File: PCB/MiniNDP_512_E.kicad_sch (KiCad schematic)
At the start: 17 parts, among them J1 Conn_02x20_Odd_Even, U1 HC138, U2 4040, U3 FCT821, U4 AS6C4008, U5 2G04, U6 1G32

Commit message: E board
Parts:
- removed C4, C5: 1u, 000_LOCAL:C_0805, symbol 000_LOCAL:C
- removed U2: 4040, 000_LOCAL:SOIC-16_3.9x9.9mm_P1.27mm, symbol 000_LOCAL:4040
- removed U3: FCT821, 000_LOCAL:SOIC-24, symbol 000_LOCAL:74xx821
- removed U4: AS6C4008, 000_LOCAL:TSOP-II-SOP-32_dual, symbol 000_LOCAL:AS6C4008_DIP
- removed U5: 2G04, 000_LOCAL:SOT-363_SC-70-6, symbol 000_LOCAL:2G04
- added C2, C3, C6, C7: 1u, 000_LOCAL:C_0805, symbol 000_LOCAL:C
- added JP1: 256k, 000_LOCAL:SolderJumper-2_Open 0.65mm, symbol 000_LOCAL:SolderJumper_2_Open
- added U1, U2, U3: HC161, 000_LOCAL:TSSOP-16, symbol 000_LOCAL:74xx161
- added U5: 74xx574, 000_LOCAL:TSSOP-20, symbol 000_LOCAL:74xx574
- added U6: AS6C4008, 000_LOCAL:TSOP32-dual, symbol 000_LOCAL:AS6C4008_TSOP
- added U8: 1G79, 000_LOCAL:SOT-353_SC-70-5, symbol 000_LOCAL:74xx1G79
- U4: renamed from U1; footprint 000_LOCAL:SOIC-16_3.9x9.9mm_P1.27mm -> 000_LOCAL:TSSOP-16
- renumbered C2 to C4, C3 to C5, U6 to U7
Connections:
- net A0: now also U1.14 (Q0), U6.15 (A5)
- net A1: now also U1.13 (Q1), U6.14 (A6)
- net A10: now also U5.19 (Q0), U6.11 (A14)
- net A11: now also U5.18 (Q1), U6.10 (A16)
- net A12: now also U5.17 (Q2), U6.7 (A15)
- net A13: now also U5.16 (Q3), U6.4 (A13)
- net A14: now also U5.15 (Q4), U6.3 (A8)
- net A15: now also U5.14 (Q5), U6.2 (A9)
- net A16: now also U5.13 (Q6), U6.1 (A11)
- net A17: now also U5.12 (Q7), U6.9 (A18)
- net A18: now also JP1.2 (B), U6.6 (A17), U8.4 (Q)
- net A2: now also U1.12 (Q2), U6.13 (A7)
- net A3: now also U1.11 (Q3), U6.12 (A12)
- net A4: now also U2.14 (Q0), U6.19 (A1)
- net A5: now also U2.13 (Q1), U6.20 (A0)
- net A6: now also U2.12 (Q2), U6.31 (A10)
- net A7: now also U2.11 (Q3), U6.16 (A4)
- net A8: now also U3.14 (Q0), U6.17 (A3)
- net A9: now also U3.13 (Q1), U6.18 (A2)
- net AD0: now also U5.2 (D0), U6.21 (Q0)
- net AD1: now also U5.3 (D1), U6.22 (Q1)
- net AD2: now also U5.4 (D2), U6.23 (Q2)
- net AD3: now also U5.5 (D3), U6.25 (Q3)
- net AD4: now also U5.6 (D4), U6.26 (Q4)
- net AD5: now also U5.7 (D5), U6.27 (Q5)
- net AD6: now also U5.8 (D6), U6.28 (Q6)
- net AD7: now also U5.9 (D7), U6.29 (Q7)
- net BUS_A10: now also U8.1 (D)
- net GND: now also U4.4 (E1), C2.2, C3.2, C6.2, C7.2, U1.3 (D0), U1.4 (D1), U1.5 (D2), U1.6 (D3), U1.8 (GND), U2.3 (D0), U2.4 (D1), U2.5 (D2), U2.6 (D3), U2.8 (GND), U3.3 (D0), U3.4 (D1), U3.5 (D2), U3.6 (D3), U3.8 (GND), U5.1 (OE), U5.10 (GND), U6.24 (GND), U8.3 (GND); no longer U4.5 (E2)
- net SLEEP: now also U7.2; no longer U7.1
- net VBUS: now also C3.1, C6.1, C7.1, JP1.1 (A), U1.10 (CET), U1.16 (VCC), U1.7 (CEP), U1.9 (~{PE}), U2.16 (VCC), U2.9 (~{PE}), U3.16 (VCC), U3.9 (~{PE}), U5.20 (VCC), U8.5 (VCC)
- net VMEM: now also C2.1, U6.8 (VCC)
- net ~{BLOCK}: now also U1.1 (~{MR}), U2.1 (~{MR}), U3.1 (~{MR}), U5.11 (Cp), U8.2 (C)
- net ~{BYTE}: now also U7.1, U1.2 (CP), U2.2 (CP), U3.2 (CP); no longer U7.2
- net ~{CE}: now also U6.30 (~{CE})
- net ~{RD}: now also U6.32 (~{OE})
- net ~{WR}: now also U6.5 (~{WE})
- net ~{Y0}: now also U4.5 (E2); no longer U4.4 (E1)
- new net TC0: U1.15 (TC), U2.10 (CET), U2.7 (CEP)
- new net TC1: U2.15 (TC), U3.10 (CET), U3.7 (CEP)
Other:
- note added: "(*)"
- note added: "(*) A17 must be opposite AD7 for 128k compatibility"
- note added: "(**)"
- note added: "(**) A18 must be on pin 6 for 256k or 128k compatibility A17 must be on pin 9 for 128k compatibility"
- note added: "For 512k: Populate U8 with 1G79 or 1G80. Keep JP1 Open. Populate U6 with AS6C4008. For 256k or 128k: Don't populate U8. Bridge JP1. Populate U6 with AS6C2008A or AS6C1008."
- note added: "GND"
- note added: "TANDY 100/102/200 BUS (A) ~{YO} A8 A9 A10 -> ~{BLOCK} ~{BYTE} L X X X X X X X H X X X X X X X L X X X X H L H L L -> L H Select BLOCK # from BANK0 H L H L H -> L H Select BLOCK # from BANK1 H L H H X -> H L READ/WRITE BYTE Each ~{BLOCK} pulse low: sets A0-A9 to 0, sets A10-A18 from AD0-AD7 & BUS_A10, then holds A10-A18 latched while high. Each ~{BYTE} pulse low: enables SRAM for read or write whi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"
- note removed: "A19"
- note removed: "SOP-32 or TSOP-II-32"
- note removed: "TANDY 100/102/200 BUS (A) ~{YO} A8 A9 A10 -> ~{BLOCK} ~{BYTE} L X X X X X X X H X X X X X X X L X X X X H L H L L -> L H Select BLOCK # from BANK0 H L H L H -> L H Select BLOCK # from BANK1 H L H H X -> H L READ/WRITE BYTE Each ~{BLOCK} pulse low: sets SRAM A0-A9 to 0 sets SRAM A10-A19 from BUS AD0-AD7 & A10 (AD0-AD7 = block#, BUS_A10 = bank#) On returning high: holds SRAM A10-A19 latched while h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"
- moved on the sheet: BT1, C1, C4, C5, DA1A, DA1B, J1, R1, R2, U4, U7

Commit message: E board
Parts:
- U5: value 74xx574 -> HC574
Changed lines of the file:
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@@
 			)
 		)
-		(property "Value" "74xx574"
+		(property "Value" "HC574"
 			(at 154.5941 97.79 0)
 			(effects
@@
 			)
 		)
-		(property "Datasheet" "http://www.ti.com/lit/gpn/sn74LS574"
+		(property "Datasheet" "datasheets/HC574.pdf"
 			(at 152.4 115.57 0)
 			(effects

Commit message: E board
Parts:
- removed C6, C7: 1u, 000_LOCAL:C_0805, symbol 000_LOCAL:C
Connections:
- net BUS_A8: now also U4.3 (A2); no longer U4.1 (A0)
- net GND: now also U4.1 (A0), U4.5 (E2); no longer U4.3 (A2), U4.4 (E1)
- net ~{BLOCK}: now also U4.11 (O4); no longer U4.14 (O1)
- net ~{BYTE}: now also U4.9 (O6); no longer U4.12 (O3)
- net ~{Y0}: now also U4.4 (E1); no longer U4.5 (E2)
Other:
- moved on the sheet: C3, C4, C5, U4

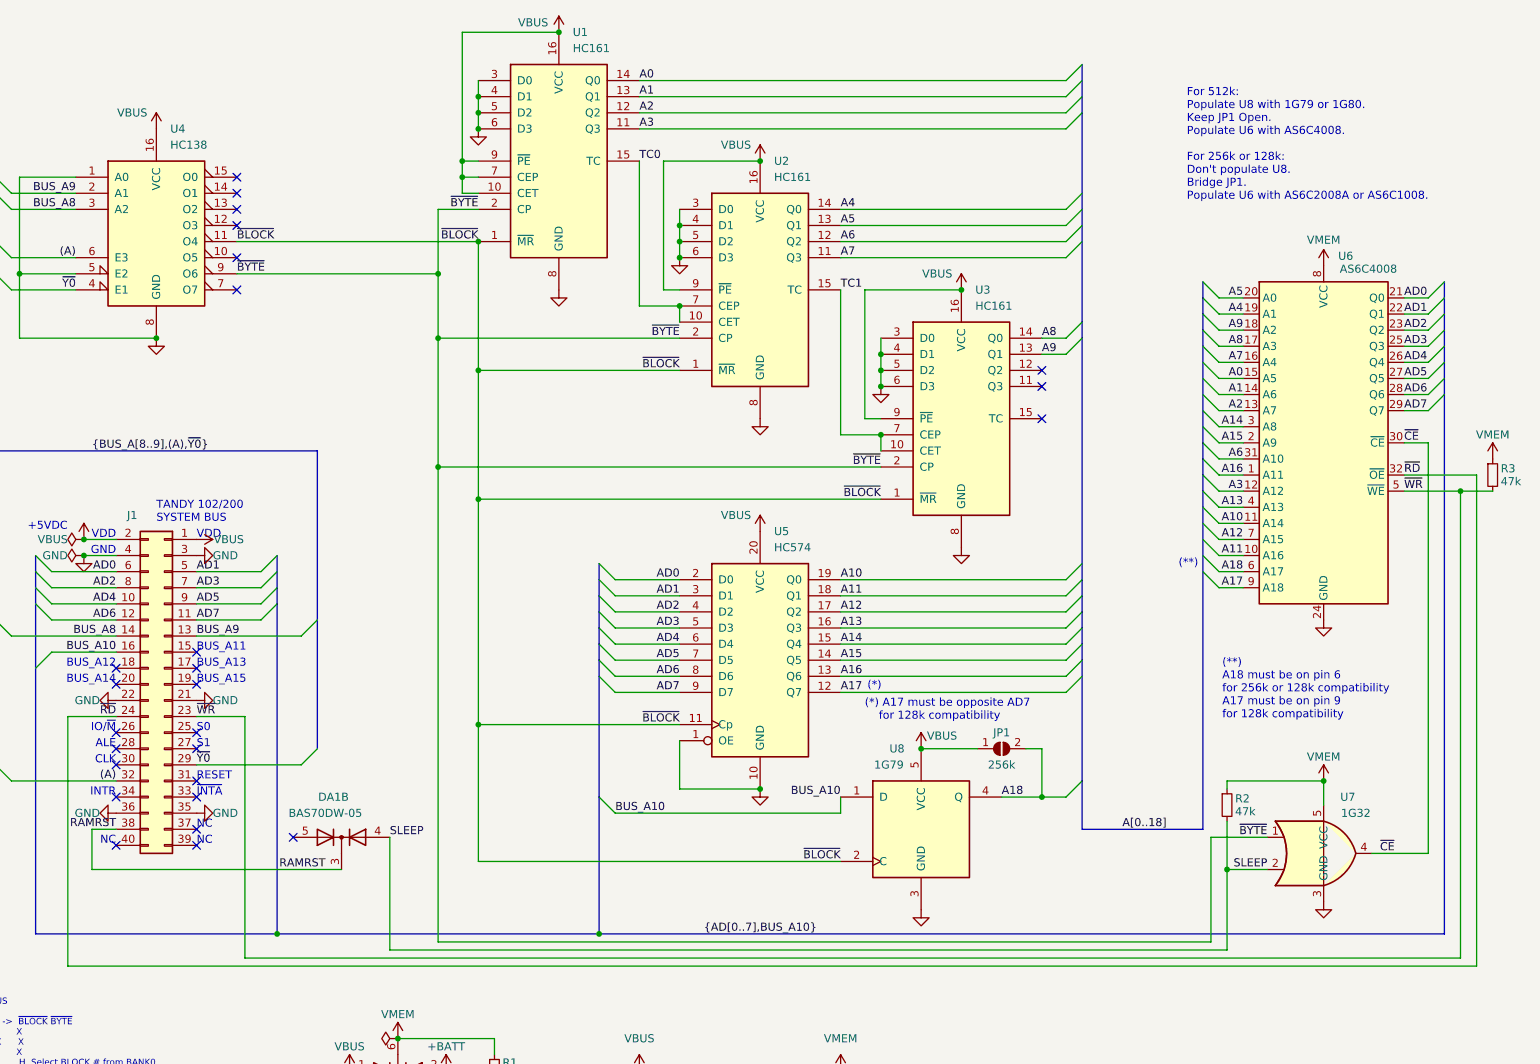
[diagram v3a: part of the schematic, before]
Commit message: E board minor trace positions
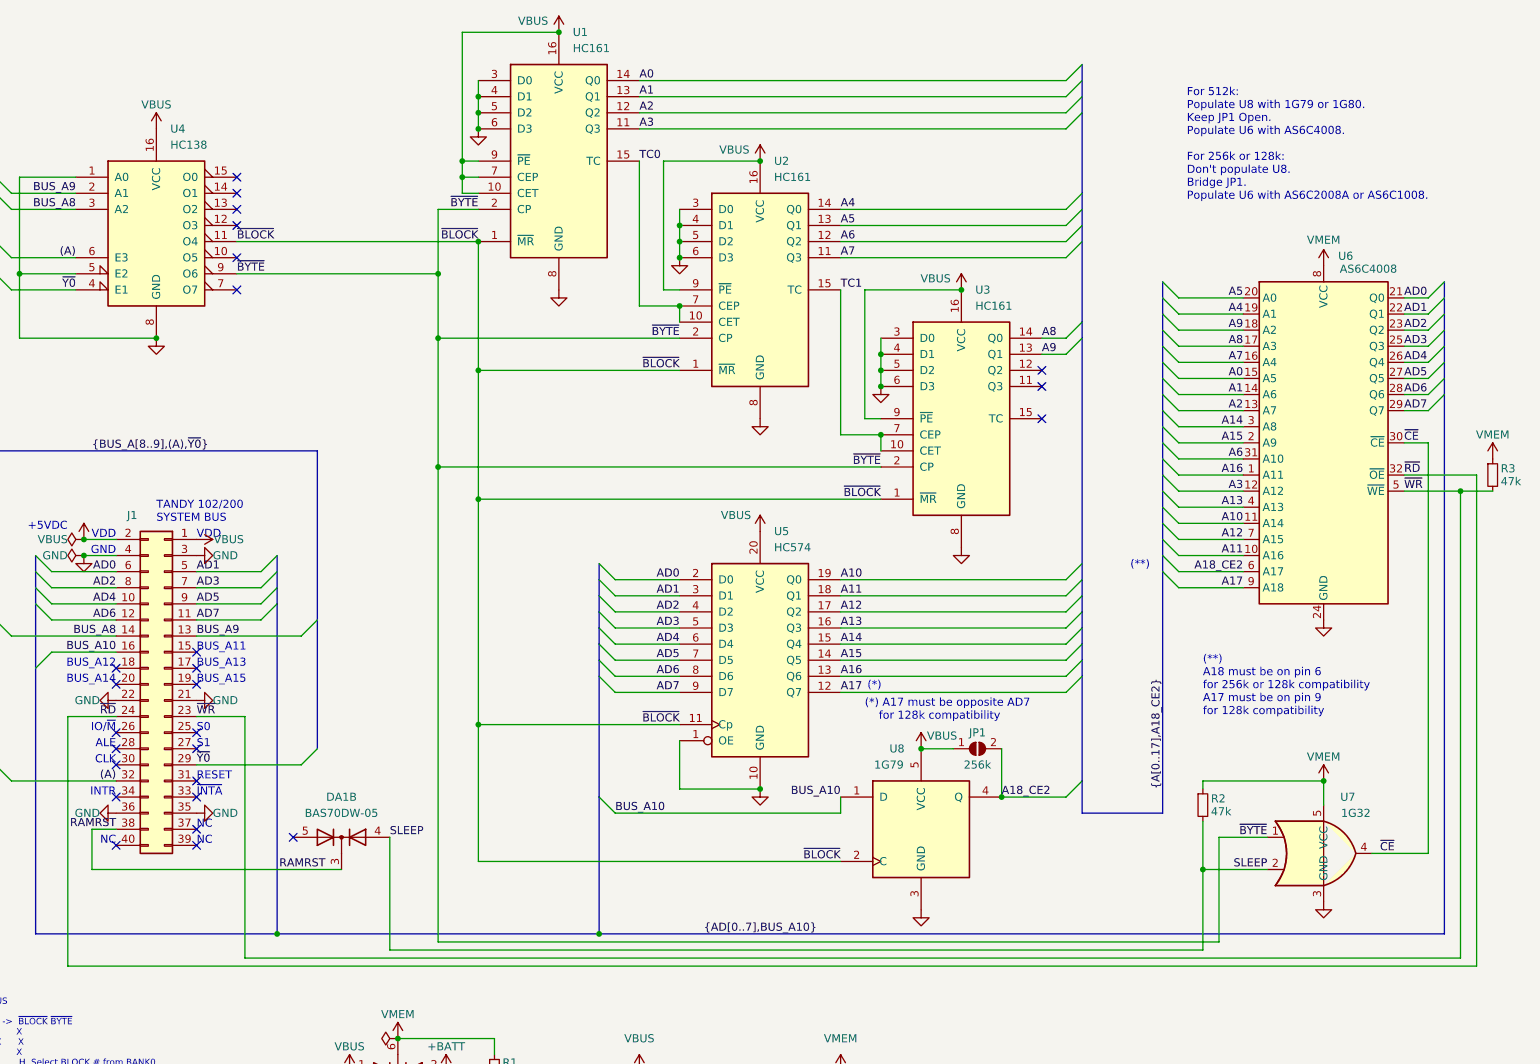
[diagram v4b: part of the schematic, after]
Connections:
- net A18 renamed A18_CE2
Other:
- moved on the sheet: JP1, R2

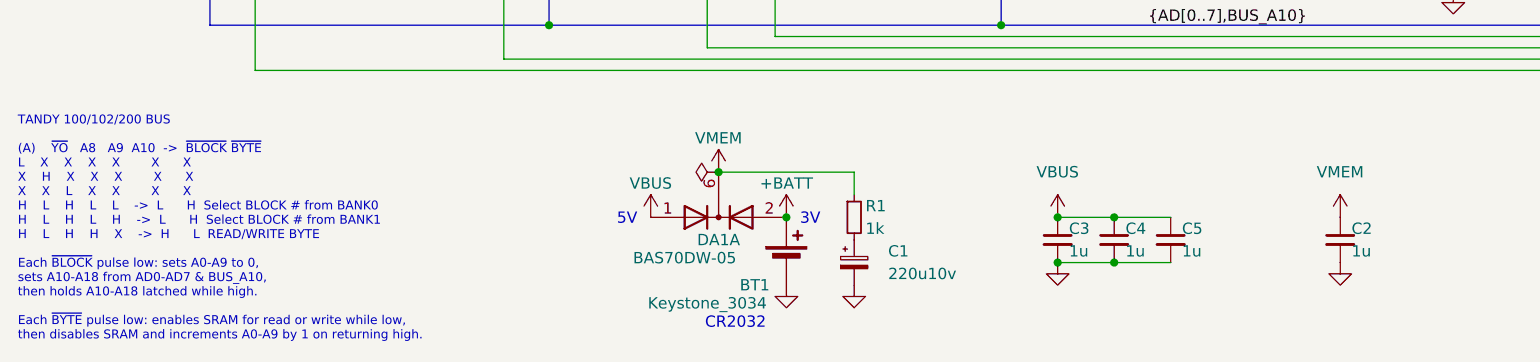
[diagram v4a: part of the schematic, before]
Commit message: 512_E & 1M silkscreen, MPNs in sch, pos & bom
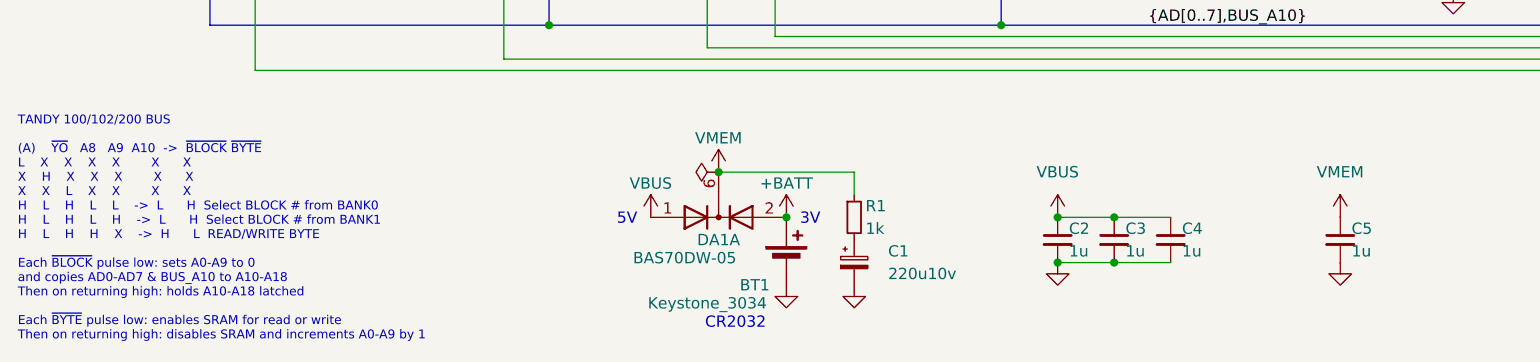
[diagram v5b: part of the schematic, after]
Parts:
- BT1: MPN (none) -> Keystone 3034
- C1: MPN (none) -> TAJC227K010RNJ
- C2, C3, C4, C5: MPN (none) -> CL21B105KAFNNNE
- DA1: MPN (none) -> BAS70DW-05-7-F
- J1: MPN (none) -> 302-S401
- JP1: now left out of the parts list
- R1: MPN (none) -> RK73B2ATTD102J
- R2, R3: MPN (none) -> RMCF0805FT47K0
- U1, U2, U3: MPN (none) -> 74HC161PW,118
- U4: MPN (none) -> 74HC138PW,118
- U5: MPN (none) -> 74HC574PW,118
- U6: MPN (none) -> AS6C4008-55STIN
- U7: MPN (none) -> 74LVC1G32GW,125
- U8: MPN (none) -> 74LVC1G79GW,125
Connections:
- net VBUS: now also C2.1; no longer C5.1
- net VMEM: now also C5.1; no longer C2.1
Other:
- note added: "TANDY 100/102/200 BUS (A) ~{YO} A8 A9 A10 -> ~{BLOCK} ~{BYTE} L X X X X X X X H X X X X X X X L X X X X H L H L L -> L H Select BLOCK # from BANK0 H L H L H -> L H Select BLOCK # from BANK1 H L H H X -> H L READ/WRITE BYTE Each ~{BLOCK} pulse low: sets A0-A9 to 0 and copies AD0-AD7 & BUS_A10 to A10-A18 Then on returning high: holds A10-A18 latched Each ~{BYTE} pulse low: enables SRAM for read or 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"
- note removed: "TANDY 100/102/200 BUS (A) ~{YO} A8 A9 A10 -> ~{BLOCK} ~{BYTE} L X X X X X X X H X X X X X X X L X X X X H L H L L -> L H Select BLOCK # from BANK0 H L H L H -> L H Select BLOCK # from BANK1 H L H H X -> H L READ/WRITE BYTE Each ~{BLOCK} pulse low: sets A0-A9 to 0, sets A10-A18 from AD0-AD7 & BUS_A10, then holds A10-A18 latched while high. Each ~{BYTE} pulse low: enables SRAM for read or write whi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"
